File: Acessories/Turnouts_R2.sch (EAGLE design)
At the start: 197 parts, among them IC1 MCP23008/P, IC2 LTC485S, IC4 MCP23008/P, J1 AVR_SPI_PROG_3X2NS, J3 4P-2.0, J4 RJ11, J5 RJ11, J6 RJ11, J7 RJ11, M1 XL6009, Q1 BD679, Q10 BD679, Q11 BD679, Q12 BD679, Q13 BD679, Q14 BD679, Q15 BD679, Q16 BD679, Q17 BSS123, Q18 BD679, Q2 BD679, Q3 BD679, Q4 BD679, Q5 BD679, Q6 BD679, Q7 BD679, Q8 BD679, Q9 BD679, T1 BC847, U3 ATMEGA1284P, X1 MKDSN1,5/4-5,08, X10 1751303, X2 1751280, X3 1751280, X4 1751248, X5 1751280, X6 1751280, X7 1751303, X8 1751303, X9 1751303, Y1 HC49UP

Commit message: Add files via upload
Added learn switch, modified the CDU and  2 x 8 distribution strip for DCC to sections
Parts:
- removed LED20: Amber, adafruit:LED3MM
- removed M1: XL6009, GJR:XL6009
- removed R58: 3K3, rcl:R-EU_R0805
- removed X4: 1751248, con-phoenix-350:1751248
- added S1: (no value), adafruit:EG1218S
- added X11: MKKDS1/8-3,5, con-phoenix-350:MKKDS1/8-3,5
- D24, D26: value MBRS340T3 -> (none); device diode:MBRS340T3 -> diode:SCHOTTKY-DIODESMD
- R8: value 0.22R -> 10K; device rcl:R-EU_R2512 -> rcl:R-EU_R0805
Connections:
- removed net +18V: LED23.A, M1.OUT+, R68.1, R71.2
- removed net N$35: LED20.C, R58.2
- removed net OC1-2: Q1.E, Q3.E, R8.2, U3.(PC17/ADC7)PA7/D14/A0
- new net LEARN: R8.1, S1.P, U3.(PC17/ADC7)PA7/D14/A0
- net +15V: now also R68.1, R71.2; no longer M1.IN+
- net +5V: now also R8.2
- net CDU: now also LED23.A; no longer LED20.A
- net GND: now also Q1.E, Q3.E, S1.S; no longer M1.IN-, M1.OUT-, R58.1, R8.1
- net T1F: now also X11-1.K, X11-11.K, X11-13.K, X11-15.K, X11-3.K, X11-5.K, X11-7.K, X11-9.K; no longer X4-1.K
- net TRACK2: now also X11-10.K, X11-12.K, X11-14.K, X11-16.K, X11-2.K, X11-4.K, X11-6.K, X11-8.K; no longer X4-2.K
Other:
- moved on the sheet: D18, LED23, Q17, R39, R41, R73, R8

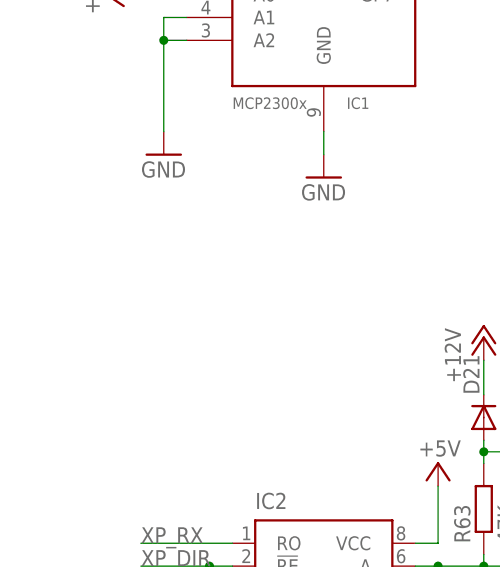
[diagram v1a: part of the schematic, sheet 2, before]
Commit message: Add files via upload
Added Turntable board based on Nano
Added learn switch to Turnouts board, moved parts to allow for DC/DC modules
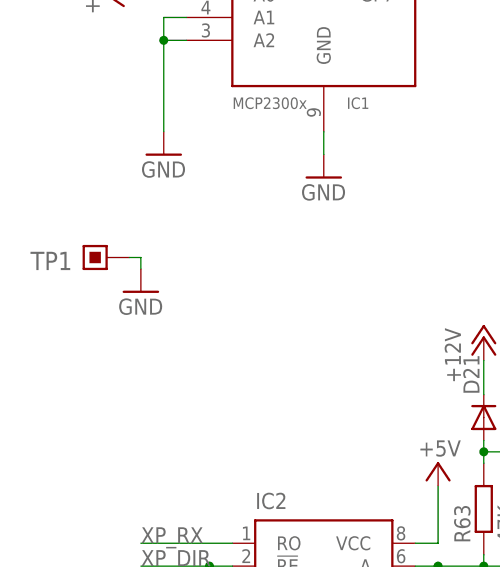
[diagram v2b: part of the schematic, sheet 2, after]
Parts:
- added TP1: (no value), RCLDT:TP1.5RUND
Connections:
- net DCCIN: now also U3.(PCI10/AIN0/INT2)PB2/D6; no longer U3.(PCI28/XCK1/OC1B)PD4/D30
- net ENT7B: now also U3.(PCI28/XCK1/OC1B)PD4/D30; no longer U3.(PCI10/AIN0/INT2)PB2/D6
- net GND: now also S1.O, TP1.1; no longer S1.S
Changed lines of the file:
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@@
 <clearance class="1" value="0.205"/>
 </class>
+<class number="2" name="gnd" width="0.2" drill="0.3">
+<clearance class="2" value="0.2"/>
+</class>
 </classes>
 <parts>
@@
 <part name="R8" library="rcl" deviceset="R-EU_" device="R0805" value="10K"/>
 <part name="P+8" library="supply1" deviceset="+5V" device=""/>
+<part name="TP1" library="RCLDT" deviceset="TP" device="1.5RUND"/>
+<part name="GND60" library="supply1" deviceset="GND" device=""/>
 </parts>
 <sheets>
@@
 </segment>
 <segment>
-<pinref part="S1" gate="1" pin="S"/>
-<wire x1="234.95" y1="97.79" x2="237.49" y2="97.79" width="0.1524" layer="91"/>
-<wire x1="237.49" y1="97.79" x2="237.49" y2="96.52" width="0.1524" layer="91"/>
 <pinref part="GND25" gate="1" pin="GND"/>
+<pinref part="S1" gate="1" pin="O"/>
+<wire x1="234.95" y1="102.87" x2="237.49" y2="102.87" width="0.1524" layer="91"/>
+<wire x1="237.49" y1="102.87" x2="237.49" y2="96.52" width="0.1524" layer="91"/>
 </segment>
 </net>
@@
 </segment>
 <segment>
-<pinref part="U3" gate="G$1" pin="(PCI10/AIN0/INT2)PB2/D6"/>
-<wire x1="200.66" y1="64.77" x2="213.36" y2="64.77" width="0.1524" layer="91"/>
-<label x="207.01" y="64.77" size="1.778" layer="95"/>
+<pinref part="U3" gate="G$1" pin="(PCI28/XCK1/OC1B)PD4/D30"/>
+<wire x1="200.66" y1="24.13" x2="213.36" y2="24.13" width="0.1524" layer="91"/>
+<label x="208.28" y="24.13" size="1.778" layer="95"/>
 </segment>
 </net>
@@
 </segment>
 <segment>
-<pinref part="U3" gate="G$1" pin="(PCI28/XCK1/OC1B)PD4/D30"/>
-<wire x1="200.66" y1="24.13" x2="213.36" y2="24.13" width="0.1524" layer="91"/>
-<label x="208.28" y="24.13" size="1.778" layer="95"/>
+<pinref part="U3" gate="G$1" pin="(PCI10/AIN0/INT2)PB2/D6"/>
+<wire x1="200.66" y1="64.77" x2="213.36" y2="64.77" width="0.1524" layer="91"/>
+<label x="207.01" y="64.77" size="1.778" layer="95"/>
 </segment>
 </net>
@@
 </instance>
 <instance part="P+7" gate="1" x="187.96" y="71.12" smashed="yes"/>
+<instance part="TP1" gate="G$1" x="16.51" y="95.25" smashed="yes" rot="R90">
+<attribute name="NAME" x="12.7" y="95.885" size="2.032" layer="95" rot="R180"/>
+</instance>
+<instance part="GND60" gate="1" x="20.32" y="91.44" smashed="yes">
+<attribute name="VALUE" x="17.78" y="88.9" size="1.778" layer="96"/>
+</instance>
 </instances>
 <busses>
@@
 <wire x1="223.52" y1="34.29" x2="223.52" y2="38.1" width="0.1524" layer="91"/>
 </segment>
+<segment>
+<pinref part="TP1" gate="G$1" pin="1"/>
+<pinref part="GND60" gate="1" pin="GND"/>
+<wire x1="19.05" y1="95.25" x2="20.32" y2="95.25" width="0.1524" layer="91"/>
+<wire x1="20.32" y1="95.25" x2="20.32" y2="93.98" width="0.1524" layer="91"/>
+</segment>
 </net>

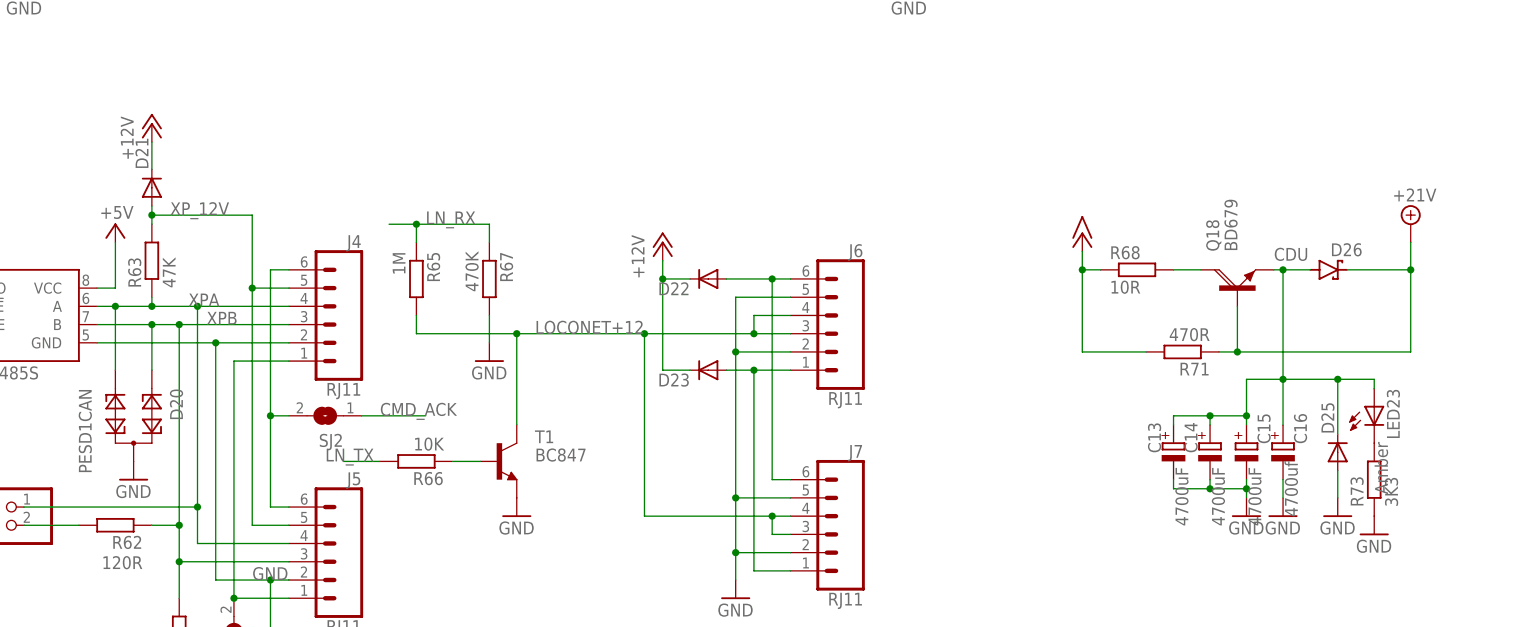
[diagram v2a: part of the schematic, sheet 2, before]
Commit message: Add files via upload
Changed Diodes on Turnouts board to SMP
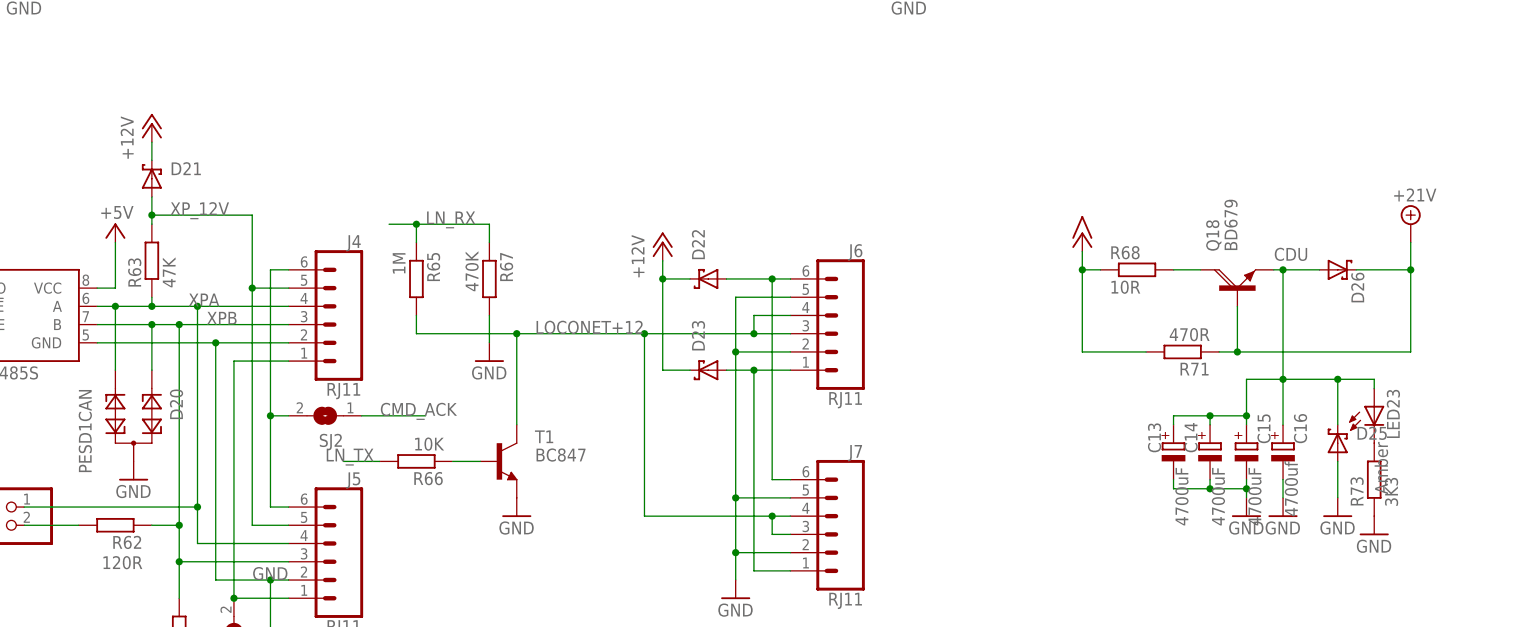
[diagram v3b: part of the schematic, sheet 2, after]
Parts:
- D21, D22, D23, D25: value CGRM4002-G -> MICROSMD-SCHOTTKY-DIODESMP; device diode:CGRM4002-G -> GJR:MICROSMD-SCHOTTKY-DIODESMP
- D24, D26: value (none) -> MICROSMD-SCHOTTKY-DIODESMP; device diode:SCHOTTKY-DIODESMD -> GJR:MICROSMD-SCHOTTKY-DIODESMP
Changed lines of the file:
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@@
 <?xml version="1.0" encoding="utf-8"?>
 <!DOCTYPE eagle SYSTEM "eagle.dtd">
-<eagle version="9.4.0">
+<eagle version="9.4.2">
 <drawing>
 <settings>
@@
 <part name="LED21" library="adafruit" library_urn="urn:adsk.eagle:library:420" deviceset="LED" device="3MM" value="Green"/>
 <part name="LED22" library="adafruit" library_urn="urn:adsk.eagle:library:420" deviceset="LED" device="3MM" value="Amber"/>
-<part name="D26" library="diode" library_urn="urn:adsk.eagle:library:210" deviceset="SCHOTTKY-DIODE" device="SMD" package3d_urn="urn:adsk.eagle:package:43404/2"/>
+<part name="D26" library="GJR" deviceset="MICROSMD-SCHOTTKY-DIODE" device="SMP"/>
 <part name="C16" library="rcl" deviceset="CPOL-EU" device="E7.5-16" value="4700uf"/>
 <part name="C15" library="rcl" deviceset="CPOL-EU" device="E7.5-16" value="4700uF"/>
 <part name="GND57" library="supply1" deviceset="GND" device=""/>
 <part name="GND58" library="supply1" deviceset="GND" device=""/>
-<part name="D25" library="diode" library_urn="urn:adsk.eagle:library:210" deviceset="CGRM400*-G" device="" package3d_urn="urn:adsk.eagle:package:43457/2" technology="2"/>
+<part name="D25" library="GJR" deviceset="MICROSMD-SCHOTTKY-DIODE" device="SMP"/>
 <part name="SUPPLY20" library="supply2" library_urn="urn:adsk.eagle:library:372" deviceset="+21V" device=""/>
 <part name="Q18" library="transistor-power" library_urn="urn:adsk.eagle:library:400" deviceset="BD679" device="" package3d_urn="urn:adsk.eagle:package:29483/1"/>
@@
 <part name="J7" library="SparkFun-Connectors" library_urn="urn:adsk.eagle:library:513" deviceset="RJ11-6" device="" package3d_urn="urn:adsk.eagle:package:38232/1" value="RJ11"/>
 <part name="J6" library="SparkFun-Connectors" library_urn="urn:adsk.eagle:library:513" deviceset="RJ11-6" device="" package3d_urn="urn:adsk.eagle:package:38232/1" value="RJ11"/>
-<part name="D23" library="diode" library_urn="urn:adsk.eagle:library:210" deviceset="CGRM400*-G" device="" package3d_urn="urn:adsk.eagle:package:43457/2" technology="2"/>
-<part name="D22" library="diode" library_urn="urn:adsk.eagle:library:210" deviceset="CGRM400*-G" device="" package3d_urn="urn:adsk.eagle:package:43457/2" technology="2"/>
+<part name="D23" library="GJR" deviceset="MICROSMD-SCHOTTKY-DIODE" device="SMP"/>
+<part name="D22" library="GJR" deviceset="MICROSMD-SCHOTTKY-DIODE" device="SMP"/>
 <part name="P+19" library="supply1" library_urn="urn:adsk.eagle:library:371" deviceset="+12V" device=""/>
 <part name="R66" library="rcl" deviceset="R-EU_" device="R0805" value="10K"/>
@@
 <part name="P+20" library="supply1" deviceset="+5V" device=""/>
 <part name="P+13" library="supply1" deviceset="+5V" device=""/>
-<part name="D21" library="diode" library_urn="urn:adsk.eagle:library:210" deviceset="CGRM400*-G" device="" package3d_urn="urn:adsk.eagle:package:43457/2" technology="2"/>
+<part name="D21" library="GJR" deviceset="MICROSMD-SCHOTTKY-DIODE" device="SMP"/>
 <part name="D19" library="diode" library_urn="urn:adsk.eagle:library:210" deviceset="PESD1CAN" device="" package3d_urn="urn:adsk.eagle:package:43389/2"/>
 <part name="J1" library="SparkFun-Connectors" library_urn="urn:adsk.eagle:library:513" deviceset="AVR_SPI_PROG_3X2" device="NS" package3d_urn="urn:adsk.eagle:package:38013/1"/>
@@
 <part name="P+2" library="supply1" deviceset="+15V" device=""/>
 <part name="R71" library="rcl" deviceset="R-EU_" device="0411/12" value="470R"/>
-<part name="D24" library="diode" library_urn="urn:adsk.eagle:library:210" deviceset="SCHOTTKY-DIODE" device="SMD" package3d_urn="urn:adsk.eagle:package:43404/2"/>
+<part name="D24" library="GJR" deviceset="MICROSMD-SCHOTTKY-DIODE" device="SMP"/>
 <part name="P+7" library="supply1" deviceset="+15V" device=""/>
 <part name="X11" library="con-phoenix-350" deviceset="MKKDS1/8-3,5" device=""/>
@@
 </instance>
 <instance part="P+2" gate="1" x="58.42" y="134.62" smashed="yes"/>
-<instance part="D24" gate="G$1" x="46.99" y="129.54" smashed="yes">
-<attribute name="NAME" x="47.244" y="131.445" size="1.778" layer="95"/>
-<attribute name="VALUE" x="44.704" y="126.111" size="1.778" layer="96"/>
+<instance part="D24" gate="G$1" x="46.99" y="129.54" smashed="yes" rot="R270">
+<attribute name="NAME" x="48.895" y="129.286" size="1.778" layer="95" rot="R270"/>
 </instance>
 <instance part="X11" gate="-1" x="280.67" y="121.92" smashed="yes">
@@
 </segment>
 </net>
-<net name="CDU" class="0">
-<segment>
-<wire x1="367.03" y1="247.65" x2="367.03" y2="251.46" width="0.1524" layer="91"/>
-</segment>
-</net>
 <net name="+21V" class="0">
 <segment>
@@
 <attribute name="VALUE" x="55.88" y="74.93" size="1.778" layer="96" rot="R180"/>
 </instance>
-<instance part="D26" gate="G$1" x="222.25" y="66.04" smashed="yes">
-<attribute name="NAME" x="222.504" y="67.945" size="1.778" layer="95"/>
-<attribute name="VALUE" x="219.964" y="62.611" size="1.778" layer="96"/>
+<instance part="D26" gate="G$1" x="223.52" y="66.04" smashed="yes" rot="R270">
+<attribute name="NAME" x="225.425" y="65.786" size="1.778" layer="95" rot="R270"/>
 </instance>
 <instance part="C16" gate="G$1" x="215.9" y="41.91" smashed="yes">
@@
 <attribute name="VALUE" x="213.36" y="29.21" size="1.778" layer="96"/>
 </instance>
-<instance part="D25" gate="G$1" x="223.52" y="40.64" smashed="yes" rot="R90">
-<attribute name="NAME" x="223.0374" y="43.18" size="1.778" layer="95" rot="R90"/>
+<instance part="D25" gate="G$1" x="223.52" y="41.91" smashed="yes">
+<attribute name="NAME" x="226.06" y="42.3926" size="1.778" layer="95"/>
 </instance>
 <instance part="SUPPLY20" gate="G$1" x="233.68" y="72.39" smashed="yes">
@@
 <attribute name="NAME" x="157.48" y="67.818" size="1.778" layer="95" font="vector" rot="MR0"/>
 </instance>
-<instance part="D23" gate="G$1" x="135.89" y="52.07" smashed="yes" rot="R180">
-<attribute name="NAME" x="133.35" y="51.5874" size="1.778" layer="95" rot="R180"/>
+<instance part="D23" gate="G$1" x="135.89" y="52.07" smashed="yes" rot="R90">
+<attribute name="NAME" x="135.4074" y="54.61" size="1.778" layer="95" rot="R90"/>
 </instance>
-<instance part="D22" gate="G$1" x="135.89" y="64.77" smashed="yes" rot="R180">
-<attribute name="NAME" x="133.35" y="64.2874" size="1.778" layer="95" rot="R180"/>
+<instance part="D22" gate="G$1" x="135.89" y="64.77" smashed="yes" rot="R90">
+<attribute name="NAME" x="135.4074" y="67.31" size="1.778" layer="95" rot="R90"/>
 </instance>
 <instance part="P+19" gate="1" x="129.54" y="69.85" smashed="yes">
@@
 <attribute name="VALUE" x="13.97" y="127" size="1.778" layer="96" rot="R270"/>
 </instance>
-<instance part="D21" gate="G$1" x="58.42" y="77.47" smashed="yes" rot="R90">
-<attribute name="NAME" x="57.9374" y="80.01" size="1.778" layer="95" rot="R90"/>
+<instance part="D21" gate="G$1" x="58.42" y="78.74" smashed="yes">
+<attribute name="NAME" x="60.96" y="79.2226" size="1.778" layer="95"/>
 </instance>
 <instance part="GND48" gate="1" x="74.93" y="7.62" smashed="yes">
@@
 <pinref part="GND61" gate="1" pin="GND"/>
 <pinref part="D25" gate="G$1" pin="A"/>
-<wire x1="223.52" y1="34.29" x2="223.52" y2="38.1" width="0.1524" layer="91"/>
+<wire x1="223.52" y1="34.29" x2="223.52" y2="39.37" width="0.1524" layer="91"/>
 </segment>
 <segment>
@@
 <label x="60.96" y="73.66" size="1.778" layer="95"/>
 <pinref part="D21" gate="G$1" pin="A"/>
-<wire x1="58.42" y1="73.66" x2="58.42" y2="74.93" width="0.1524" layer="91"/>
+<wire x1="58.42" y1="73.66" x2="58.42" y2="76.2" width="0.1524" layer="91"/>
 <junction x="58.42" y="73.66"/>
 </segment>
@@
 <segment>
 <pinref part="P+17" gate="1" pin="+12V"/>
-<wire x1="58.42" y1="83.82" x2="58.42" y2="80.01" width="0.1524" layer="91"/>
+<wire x1="58.42" y1="83.82" x2="58.42" y2="81.28" width="0.1524" layer="91"/>
 <pinref part="D21" gate="G$1" pin="C"/>
 </segment>
@@
 <pinref part="D26" gate="G$1" pin="A"/>
 <wire x1="214.63" y1="66.04" x2="215.9" y2="66.04" width="0.1524" layer="91"/>
-<wire x1="215.9" y1="66.04" x2="219.71" y2="66.04" width="0.1524" layer="91"/>
+<wire x1="215.9" y1="66.04" x2="220.98" y2="66.04" width="0.1524" layer="91"/>
 <pinref part="C16" gate="G$1" pin="+"/>
 <wire x1="215.9" y1="44.45" x2="215.9" y2="50.8" width="0.1524" layer="91"/>
@@
 <wire x1="215.9" y1="50.8" x2="223.52" y2="50.8" width="0.1524" layer="91"/>
 <pinref part="D25" gate="G$1" pin="C"/>
-<wire x1="223.52" y1="50.8" x2="223.52" y2="43.18" width="0.1524" layer="91"/>
+<wire x1="223.52" y1="50.8" x2="223.52" y2="44.45" width="0.1524" layer="91"/>
 <pinref part="LED23" gate="G$1" pin="A"/>
 <wire x1="223.52" y1="50.8" x2="228.6" y2="50.8" width="0.1524" layer="91"/>
@@
 <pinref part="D26" gate="G$1" pin="C"/>
 <wire x1="209.55" y1="54.61" x2="209.55" y2="60.96" width="0.1524" layer="91"/>
-<wire x1="224.79" y1="66.04" x2="233.68" y2="66.04" width="0.1524" layer="91"/>
+<wire x1="226.06" y1="66.04" x2="233.68" y2="66.04" width="0.1524" layer="91"/>
 <wire x1="233.68" y1="66.04" x2="233.68" y2="69.85" width="0.1524" layer="91"/>
 <wire x1="209.55" y1="54.61" x2="233.68" y2="54.61" width="0.1524" layer="91"/>
